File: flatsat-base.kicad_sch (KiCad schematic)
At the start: 16 parts, among them J1 FFC2B28-24-G, J10 Conn_01x24_Male, J11 Conn_01x10_Male, J12 FFC2B28-10-G, J2 FFC2B28-10-G, J3 FFC2B28-10-G, J4 FFC2B28-10-G, J5 FFC2B28-10-G, J6 FFC2B28-10-G, J7 FFC2B28-10-G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

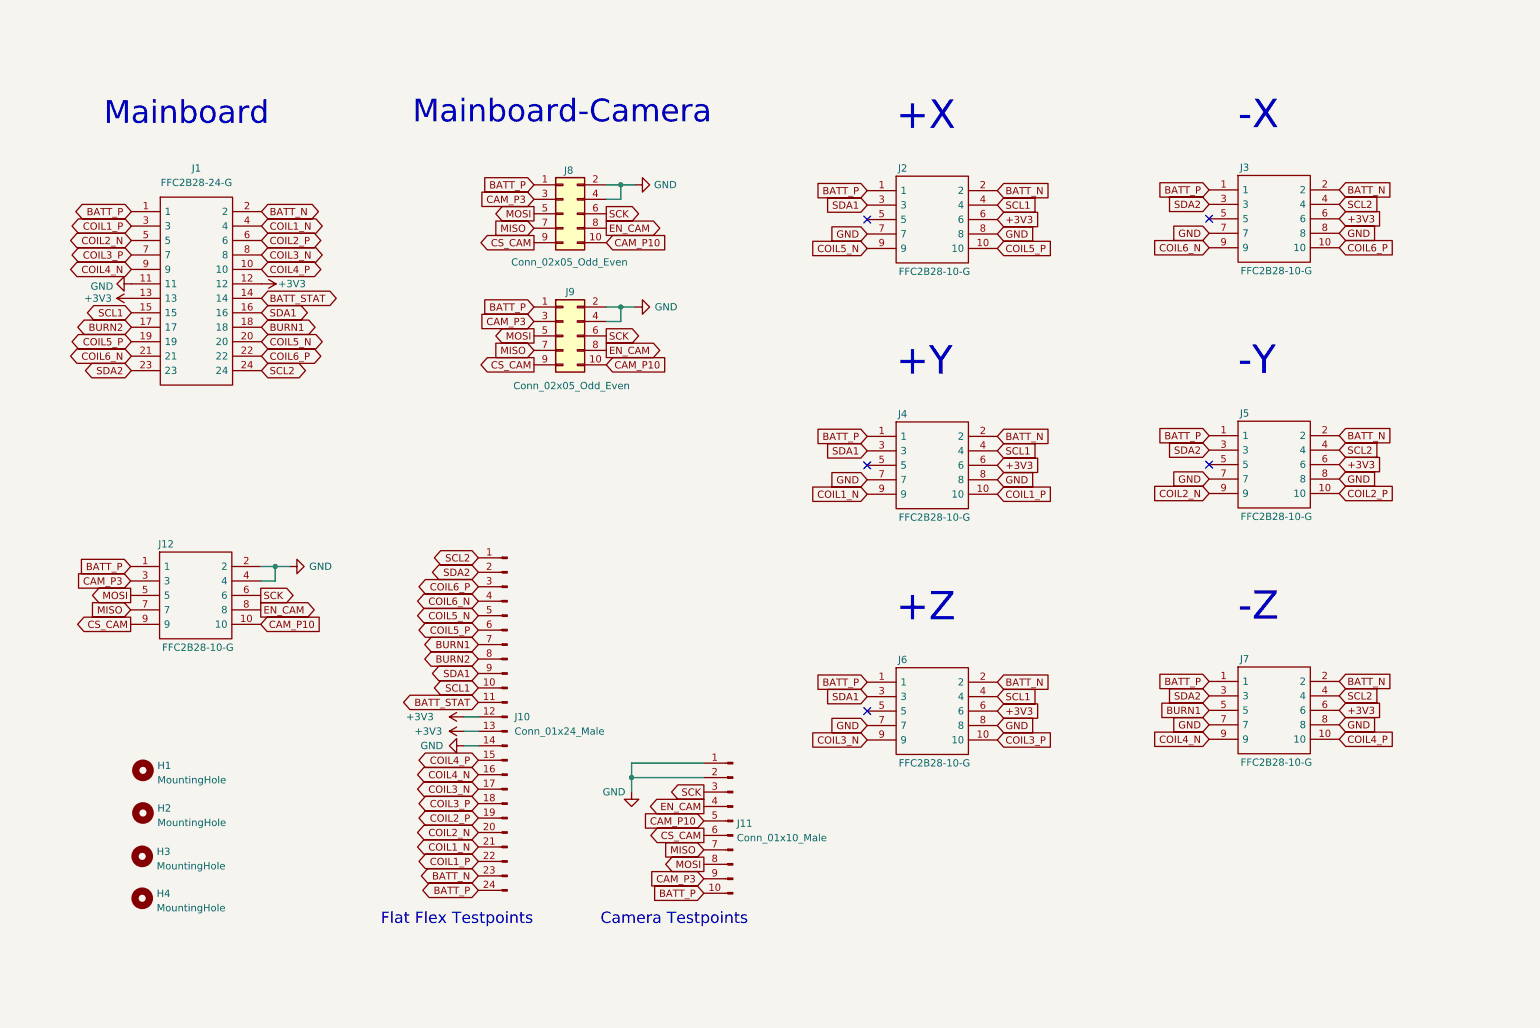
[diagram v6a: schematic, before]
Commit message: Separated Batt_P and Cam_Batt_P, added FFC connector and realigned
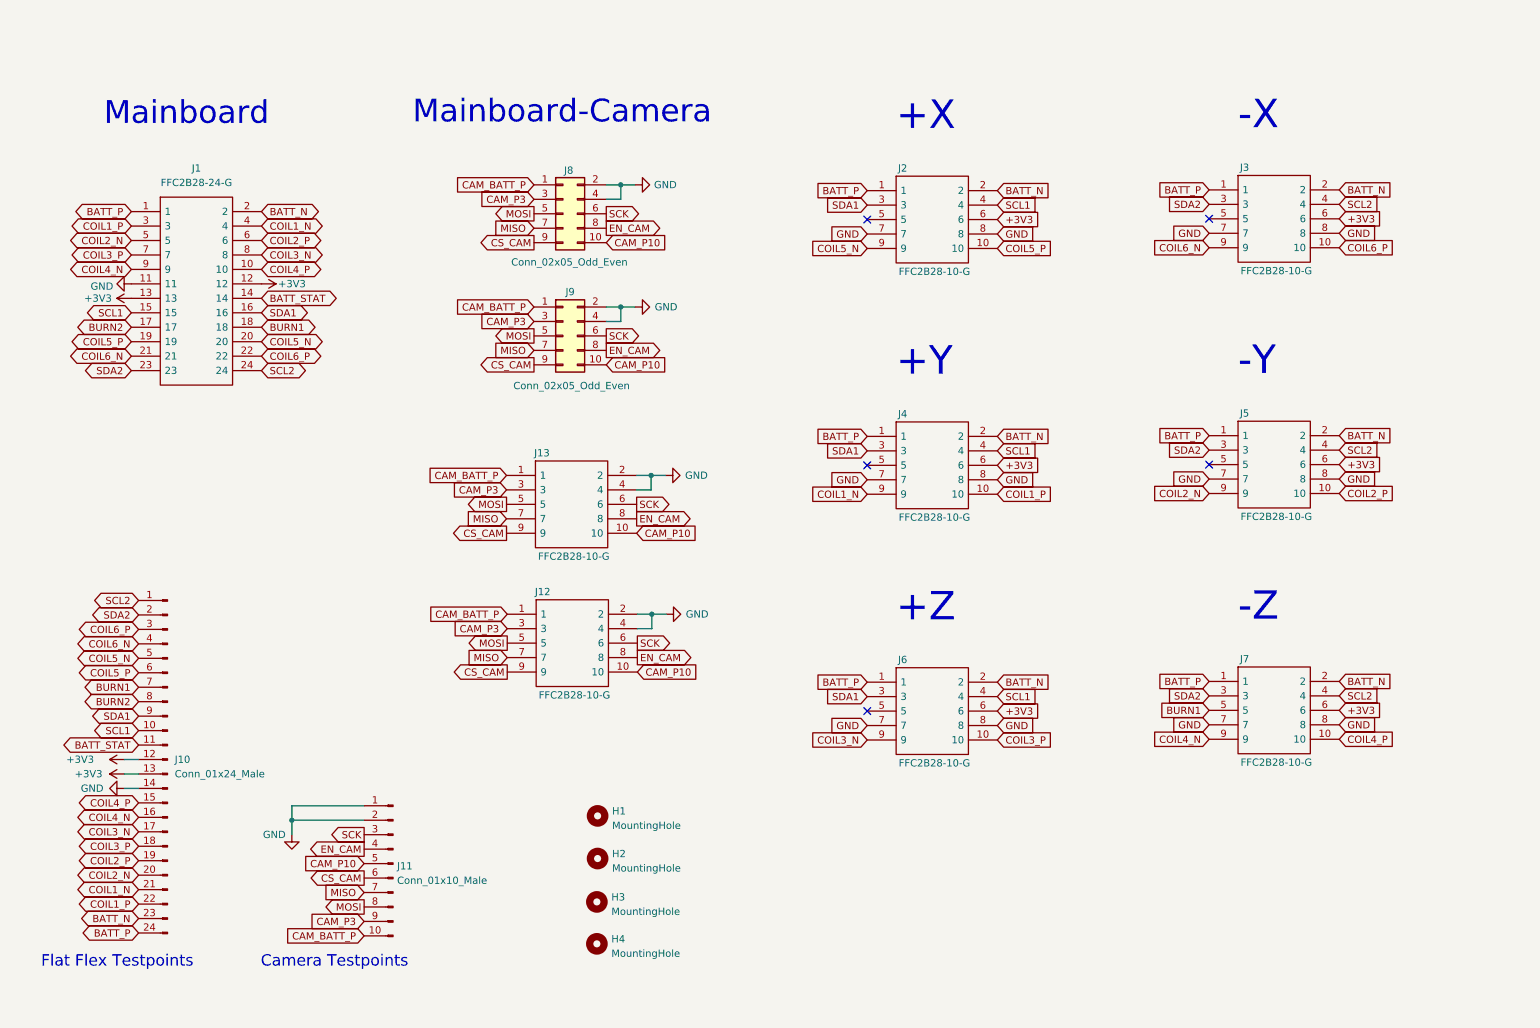
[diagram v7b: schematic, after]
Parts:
- added J13: FFC2B28-10-G, solarpanels:GCT_FFC2B28-10-G, symbol solarpanels:FFC2B28-10-G
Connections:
- net BATT_P: no longer J11.10 (Pin_10), J12.1, J8.1 (Pin_1), J9.1 (Pin_1)
- net CAM_P10: now also J13.10
- net CAM_P3: now also J13.3
- net CS_CAM: now also J13.9
- net EN_CAM: now also J13.8
- net GND: now also J13.2, J13.4
- net MISO: now also J13.7
- net MOSI: now also J13.5
- net SCK: now also J13.6
- new net CAM_BATT_P: J11.10 (Pin_10), J12.1, J13.1, J8.1 (Pin_1), J9.1 (Pin_1)
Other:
- moved on the sheet: H1, H2, H3, H4, J10, J11, J12

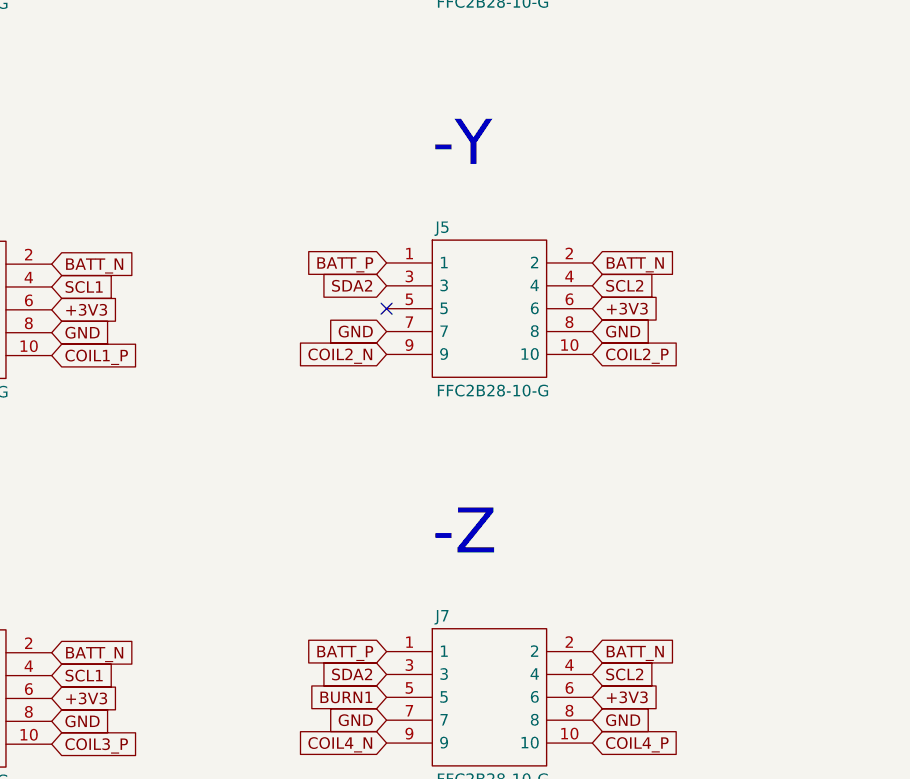
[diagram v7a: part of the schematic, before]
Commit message: add battery connector and aligator clip points
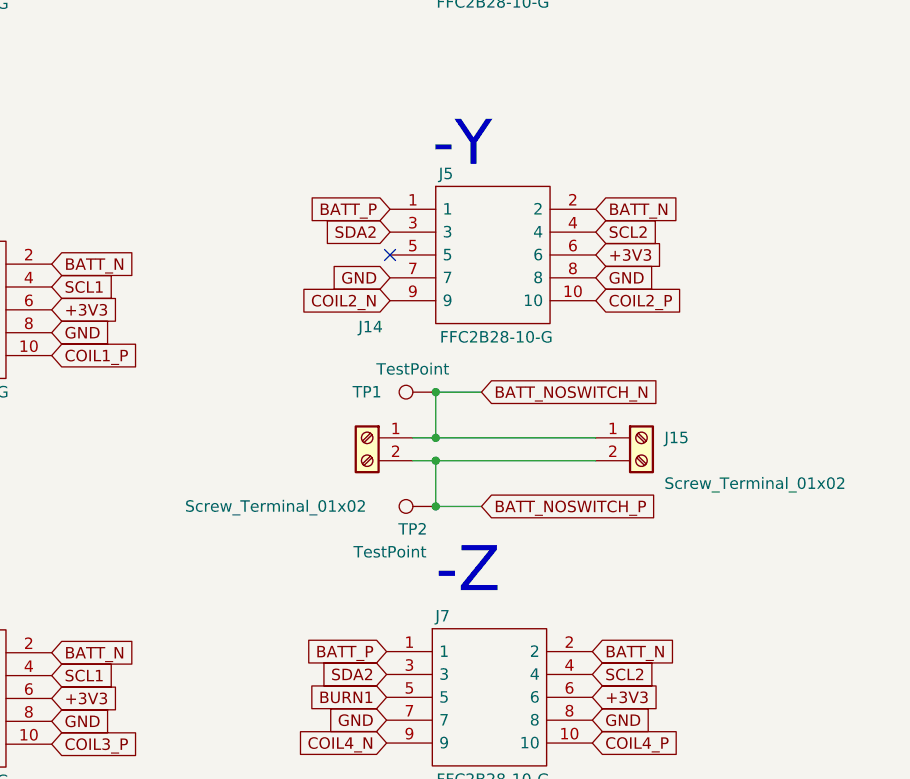
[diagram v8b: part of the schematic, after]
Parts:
- added J14, J15: Screw_Terminal_01x02, solarpanels:SCREWTERMINAL-3.5MM-2_LOCK, symbol Connector:Screw_Terminal_01x02
- added TP1, TP2: TestPoint, TestPoint:TestPoint_Plated_Hole_D5.0mm, symbol Connector:TestPoint
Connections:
- new net BATT_NOSWITCH_N: J14.1 (Pin_1), J15.1 (Pin_1), TP1.1
- new net BATT_NOSWITCH_P: J14.2 (Pin_2), J15.2 (Pin_2), TP2.1
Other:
- moved on the sheet: J5
